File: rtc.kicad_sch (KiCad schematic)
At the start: 3 parts, among them U401 DS3231MZ

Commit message: SH-RPi v2 schematic design
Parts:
- removed BT401: CR1220/3V, SH-RPi:BatteryHolder_Myoung_MY-1220-03, symbol Connector_Generic:Conn_01x03
- removed U401: DS3231MZ, Package_SO:SOIC-8_3.9x4.9mm_P1.27mm, symbol Timer_RTC:DS3231MZ
- added BT801: Battery_Cell, symbol Device:Battery_Cell
- added C801: 1uF, symbol Device:C
- added C802: 22pF C0G, symbol Device:C_Small
- added D801, D802: 1N4148WS, Diode_SMD:D_SOD-323, symbol Device:D
- added JP801: SolderJumper_2_Bridged, symbol Jumper:SolderJumper_2_Bridged
- added U801: PCF8563T, Package_SO:SOIC-8_3.9x4.9mm_P1.27mm, symbol Timer_RTC:PCF8563T
- added Y801: X1A000061000200, Crystal:Crystal_SMD_2012-2Pin_2.0x1.2mm, symbol Device:Crystal
- renumbered C401 to C803
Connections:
- net GND: now also BT801.2 (-), C801.2, C802.1, U801.4 (VSS)
- net RTC_INT: now also U801.3 (~{INT})
- net SCL: now also U801.6 (SCL)
- net SDA: now also U801.5 (SDA)
- net VBAT: now also BT801.1 (+), C801.1, D802.2 (A)
- net ATT_Vcc: no longer names the net of C803.1
- net ATT_Vcc: now also D801.1 (K), D802.1 (K), U801.8 (VDD)
- new net: C802.2, U801.1 (OSCI), Y801.2
- new net: D801.2 (A), JP801.2 (B)
- new net: U801.2 (OSCO), Y801.1
- new net +3V3: JP801.1 (A)
- no-connect marks 3 -> 1

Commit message: WIP: Assign footprints and LCSC part numbers
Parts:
- C801: footprint (none) -> Capacitor_SMD:C_0402_1005Metric; LCSC (none) -> C52923
- C802: footprint (none) -> Capacitor_SMD:C_0402_1005Metric; LCSC (none) -> C1555
- JP801: footprint (none) -> Jumper:SolderJumper-2_P1.3mm_Bridged_Pad1.0x1.5mm
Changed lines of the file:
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@@
     (property "Reference" "C802" (id 0) (at 100.3363 85.09 90))
     (property "Value" "22pF C0G" (id 1) (at 100.3363 87.63 90))
-    (property "Footprint" "" (id 2) (at 100.33 91.44 0)
+    (property "Footprint" "Capacitor_SMD:C_0402_1005Metric" (id 2) (at 100.33 91.44 0)
       (effects (font (size 1.27 1.27)) hide)
     )
     (property "Datasheet" "~" (id 3) (at 100.33 91.44 0)
+      (effects (font (size 1.27 1.27)) hide)
+    )
+    (property "LCSC" "C1555" (id 4) (at 100.33 91.44 0)
       (effects (font (size 1.27 1.27)) hide)
     )
@@
       (effects (font (size 1.27 1.27)) (justify left))
     )
-    (property "Footprint" "" (id 2) (at 51.7652 100.33 0)
+    (property "Footprint" "Capacitor_SMD:C_0402_1005Metric" (id 2) (at 51.7652 100.33 0)
       (effects (font (size 1.27 1.27)) hide)
     )
     (property "Datasheet" "~" (id 3) (at 50.8 96.52 0)
+      (effects (font (size 1.27 1.27)) hide)
+    )
+    (property "LCSC" "C52923" (id 4) (at 50.8 96.52 0)
       (effects (font (size 1.27 1.27)) hide)
     )
@@
     (property "Reference" "JP801" (id 0) (at 92.71 69.85 0))
     (property "Value" "SolderJumper_2_Bridged" (id 1) (at 92.71 72.39 0))
-    (property "Footprint" "" (id 2) (at 92.71 76.2 0)
+    (property "Footprint" "Jumper:SolderJumper-2_P1.3mm_Bridged_Pad1.0x1.5mm" (id 2) (at 92.71 76.2 0)
       (effects (font (size 1.27 1.27)) hide)
     )

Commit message: Use a battery clip instead of a cell
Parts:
- removed BT801: Battery_Cell, symbol Device:Battery_Cell
- added J801: Conn_01x03, SH-RPi:BatteryHolder_Myoung_MY-1220-03, symbol Connector_Generic:Conn_01x03
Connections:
- net GND: now also J801.3 (Pin_3)
- net VBAT: now also J801.1 (Pin_1), J801.2 (Pin_2)
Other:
- note added: "CR1220 battery"
- note added: "Cut the solder jumper to disable RTC"
- moved on the sheet: C801
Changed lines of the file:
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@@
     (comment 3 "Sailor Hat for Raspberry Pi is licensed under CC BY 4.0.")
   )
+  (junction (at 60.96 91.44) (diameter 0) (color 0 0 0 0)
+  )
   (junction (at 74.93 83.82) (diameter 0) (color 0 0 0 0)
   )
@@
   (junction (at 106.68 91.44) (diameter 0) (color 0 0 0 0)
   )
-  (junction (at 60.96 91.44) (diameter 0) (color 0 0 0 0)
-  )
   (junction (at 127 80.01) (diameter 0) (color 0 0 0 0)
   )
+  (junction (at 73.66 91.44) (diameter 0) (color 0 0 0 0)
+  )
   (no_connect (at 137.16 99.06))
+  (wire (pts (xy 57.15 93.98) (xy 60.96 93.98))
+    (stroke (width 0) (type default) (color 0 0 0 0))
+  )
   (wire (pts (xy 110.49 80.01) (xy 74.93 80.01))
     (stroke (width 0) (type default) (color 0 0 0 0))
@@
     (stroke (width 0) (type default) (color 0 0 0 0))
   )
-  (wire (pts (xy 60.96 99.06) (xy 60.96 102.87))
+  (wire (pts (xy 60.96 96.52) (xy 60.96 102.87))
     (stroke (width 0) (type default) (color 0 0 0 0))
   )
@@
     (stroke (width 0) (type default) (color 0 0 0 0))
   )
-  (wire (pts (xy 50.8 91.44) (xy 60.96 91.44))
+  (wire (pts (xy 57.15 91.44) (xy 60.96 91.44))
     (stroke (width 0) (type default) (color 0 0 0 0))
   )
@@
     (stroke (width 0) (type default) (color 0 0 0 0))
   )
-  (wire (pts (xy 50.8 100.33) (xy 50.8 102.87))
+  (wire (pts (xy 73.66 100.33) (xy 73.66 102.87))
     (stroke (width 0) (type default) (color 0 0 0 0))
   )
@@
     (stroke (width 0) (type default) (color 0 0 0 0))
   )
-  (wire (pts (xy 60.96 91.44) (xy 74.93 91.44))
-    (stroke (width 0) (type default) (color 0 0 0 0))
-  )
   (wire (pts (xy 144.78 101.6) (xy 137.16 101.6))
     (stroke (width 0) (type default) (color 0 0 0 0))
@@
     (stroke (width 0) (type default) (color 0 0 0 0))
   )
+  (wire (pts (xy 73.66 91.44) (xy 74.93 91.44))
+    (stroke (width 0) (type default) (color 0 0 0 0))
+  )
   (wire (pts (xy 132.08 76.2) (xy 128.27 76.2))
     (stroke (width 0) (type default) (color 0 0 0 0))
@@
     (stroke (width 0) (type default) (color 0 0 0 0))
   )
+  (wire (pts (xy 60.96 91.44) (xy 73.66 91.44))
+    (stroke (width 0) (type default) (color 0 0 0 0))
+  )
+  (wire (pts (xy 60.96 93.98) (xy 60.96 91.44))
+    (stroke (width 0) (type default) (color 0 0 0 0))
+  )
   (wire (pts (xy 118.11 80.01) (xy 127 80.01))
     (stroke (width 0) (type default) (color 0 0 0 0))
@@
     (stroke (width 0) (type default) (color 0 0 0 0))
   )
-  (wire (pts (xy 50.8 92.71) (xy 50.8 91.44))
+  (wire (pts (xy 73.66 92.71) (xy 73.66 91.44))
     (stroke (width 0) (type default) (color 0 0 0 0))
   )
@@
   (wire (pts (xy 102.87 91.44) (xy 106.68 91.44))
     (stroke (width 0) (type default) (color 0 0 0 0))
+  )
+  (wire (pts (xy 57.15 96.52) (xy 60.96 96.52))
+    (stroke (width 0) (type default) (color 0 0 0 0))
+  )
+  (text "Cut the solder jumper\nto disable RTC" (at 85.09 64.77 0)
+    (effects (font (size 1.27 1.27)) (justify left bottom))
+  )
+  (text "CR1220 battery" (at 40.64 102.87 0)
+    (effects (font (size 1.27 1.27)) (justify left bottom))
   )
   (label "VBAT" (at 74.93 80.01 180)
@@
   (symbol (lib_id "power:GND") (at 60.96 102.87 0) (mirror y) (unit 1)
     (in_bom yes) (on_board yes)
-    (property "Reference" "#PWR0802" (id 0) (at 60.96 109.22 0)
+    (property "Reference" "#PWR0801" (id 0) (at 60.96 109.22 0)
       (effects (font (size 1.27 1.27)) hide)
     )
@@
     (pin "2")
   )
-  (symbol (lib_id "Device:C") (at 50.8 96.52 0) (unit 1)
-    (in_bom yes) (on_board yes) (fields_autoplaced)
-    (property "Reference" "C801" (id 0) (at 54.61 95.2499 0)
-      (effects (font (size 1.27 1.27)) (justify left))
-    )
-    (property "Value" "1uF" (id 1) (at 54.61 97.7899 0)
-      (effects (font (size 1.27 1.27)) (justify left))
-    )
-    (property "Footprint" "Capacitor_SMD:C_0402_1005Metric" (id 2) (at 51.7652 100.33 0)
-      (effects (font (size 1.27 1.27)) hide)
-    )
-    (property "Datasheet" "~" (id 3) (at 50.8 96.52 0)
-      (effects (font (size 1.27 1.27)) hide)
-    )
-    (property "LCSC" "C52923" (id 4) (at 50.8 96.52 0)
+  (symbol (lib_id "Device:C") (at 73.66 96.52 0) (unit 1)
+    (in_bom yes) (on_board yes) (fields_autoplaced)
+    (property "Reference" "C801" (id 0) (at 77.47 95.2499 0)
+      (effects (font (size 1.27 1.27)) (justify left))
+    )
+    (property "Value" "1uF" (id 1) (at 77.47 97.7899 0)
+      (effects (font (size 1.27 1.27)) (justify left))
+    )
+    (property "Footprint" "Capacitor_SMD:C_0402_1005Metric" (id 2) (at 74.6252 100.33 0)
+      (effects (font (size 1.27 1.27)) hide)
+    )
+    (property "Datasheet" "~" (id 3) (at 73.66 96.52 0)
+      (effects (font (size 1.27 1.27)) hide)
+    )
+    (property "LCSC" "C52923" (id 4) (at 73.66 96.52 0)
       (effects (font (size 1.27 1.27)) hide)
     )
@@
     (pin "8")
   )
-  (symbol (lib_id "power:GND") (at 50.8 102.87 0) (mirror y) (unit 1)
-    (in_bom yes) (on_board yes)
-    (property "Reference" "#PWR0801" (id 0) (at 50.8 109.22 0)
-      (effects (font (size 1.27 1.27)) hide)
-    )
-    (property "Value" "GND" (id 1) (at 50.673 107.2642 0))
-    (property "Footprint" "" (id 2) (at 50.8 102.87 0)
-      (effects (font (size 1.27 1.27)) hide)
-    )
-    (property "Datasheet" "" (id 3) (at 50.8 102.87 0)
+  (symbol (lib_id "power:GND") (at 73.66 102.87 0) (mirror y) (unit 1)
+    (in_bom yes) (on_board yes)
+    (property "Reference" "#PWR0802" (id 0) (at 73.66 109.22 0)
+      (effects (font (size 1.27 1.27)) hide)
+    )
+    (property "Value" "GND" (id 1) (at 73.533 107.2642 0))
+    (property "Footprint" "" (id 2) (at 73.66 102.87 0)
+      (effects (font (size 1.27 1.27)) hide)
+    )
+    (property "Datasheet" "" (id 3) (at 73.66 102.87 0)
       (effects (font (size 1.27 1.27)) hide)
     )
@@
     )
     (pin "1")
+  )
+  (symbol (lib_id "Connector_Generic:Conn_01x03") (at 52.07 93.98 0) (mirror y) (unit 1)
+    (in_bom yes) (on_board yes) (fields_autoplaced)
+    (property "Reference" "J801" (id 0) (at 52.07 85.09 0))
+    (property "Value" "Conn_01x03" (id 1) (at 52.07 87.63 0))
+    (property "Footprint" "SH-RPi:BatteryHolder_Myoung_MY-1220-03" (id 2) (at 52.07 93.98 0)
+      (effects (font (size 1.27 1.27)) hide)
+    )
+    (property "Datasheet" "~" (id 3) (at 52.07 93.98 0)
+      (effects (font (size 1.27 1.27)) hide)
+    )
+    (property "LCSC" "C964818" (id 4) (at 52.07 93.98 0)
+      (effects (font (size 1.27 1.27)) hide)
+    )
+    (pin "1")
+    (pin "2")
+    (pin "3")
   )
   (symbol (lib_id "power:PWR_FLAG") (at 128.27 76.2 0) (unit 1)
@@
     (pin "1")
   )
-  (symbol (lib_id "Device:Battery_Cell") (at 60.96 96.52 0) (unit 1)
-    (in_bom yes) (on_board yes) (fields_autoplaced)
-    (property "Reference" "BT801" (id 0) (at 64.77 93.2179 0)
-      (effects (font (size 1.27 1.27)) (justify left))
-    )
-    (property "Value" "Battery_Cell" (id 1) (at 64.77 95.7579 0)
-      (effects (font (size 1.27 1.27)) (justify left))
-    )
-    (property "Footprint" "" (id 2) (at 60.96 94.996 90)
-      (effects (font (size 1.27 1.27)) hide)
-    )
-    (property "Datasheet" "~" (id 3) (at 60.96 94.996 90)
-      (effects (font (size 1.27 1.27)) hide)
-    )
-    (pin "1")
-    (pin "2")
-  )
 )

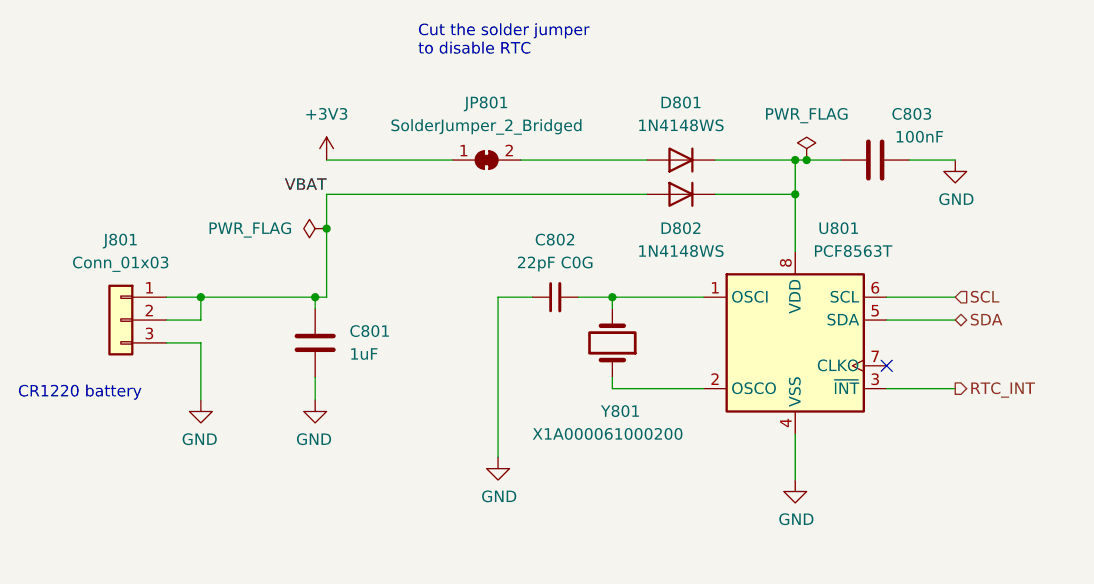
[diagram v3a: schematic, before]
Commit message: Assign footprints and part numbers to components
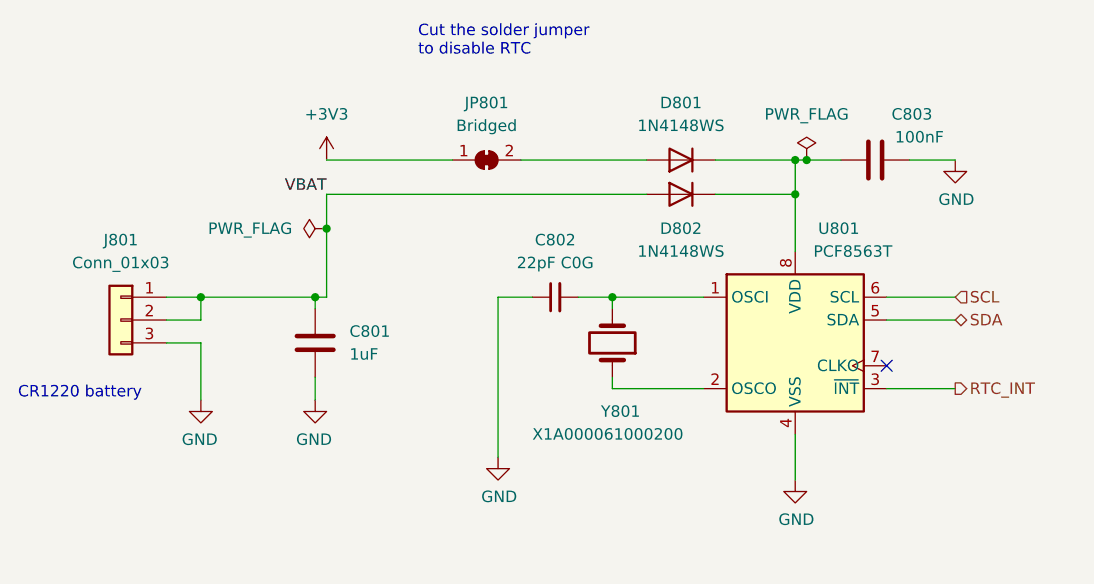
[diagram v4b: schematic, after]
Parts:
- JP801: value SolderJumper_2_Bridged -> Bridged
- U801: LCSC (none) -> C7440
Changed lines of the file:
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@@
     (in_bom yes) (on_board yes) (fields_autoplaced)
     (property "Reference" "JP801" (id 0) (at 92.71 69.85 0))
-    (property "Value" "SolderJumper_2_Bridged" (id 1) (at 92.71 72.39 0))
+    (property "Value" "Bridged" (id 1) (at 92.71 72.39 0))
     (property "Footprint" "Jumper:SolderJumper-2_P1.3mm_Bridged_Pad1.0x1.5mm" (id 2) (at 92.71 76.2 0)
       (effects (font (size 1.27 1.27)) hide)
@@
       (effects (font (size 1.27 1.27)) hide)
     )
+    (property "LCSC" "C7440" (id 4) (at 127 96.52 0)
+      (effects (font (size 1.27 1.27)) hide)
+    )

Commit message: WIP: PCB layout
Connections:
- net RTCVDD: now reaches C803.1, D801.1 (K), D802.1 (K), U801.8 (VDD)
- net OSCI: now reaches C802.2, U801.1 (OSCI), Y801.2
- net OSCO: now reaches U801.2 (OSCO), Y801.1
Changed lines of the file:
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@@
     (effects (font (size 1.27 1.27)) (justify left bottom))
+  )
+  (label "OSCO" (at 114.3 101.6 180)
+    (effects (font (size 1.27 1.27)) (justify right bottom))
   )
   (label "VBAT" (at 74.93 80.01 180)
     (effects (font (size 1.27 1.27)) (justify right bottom))
   )
+  (label "OSCI" (at 114.3 91.44 180)
+    (effects (font (size 1.27 1.27)) (justify right bottom))
+  )
+  (label "RTCVDD" (at 127 83.82 180)
+    (effects (font (size 1.27 1.27)) (justify right bottom))
+  )

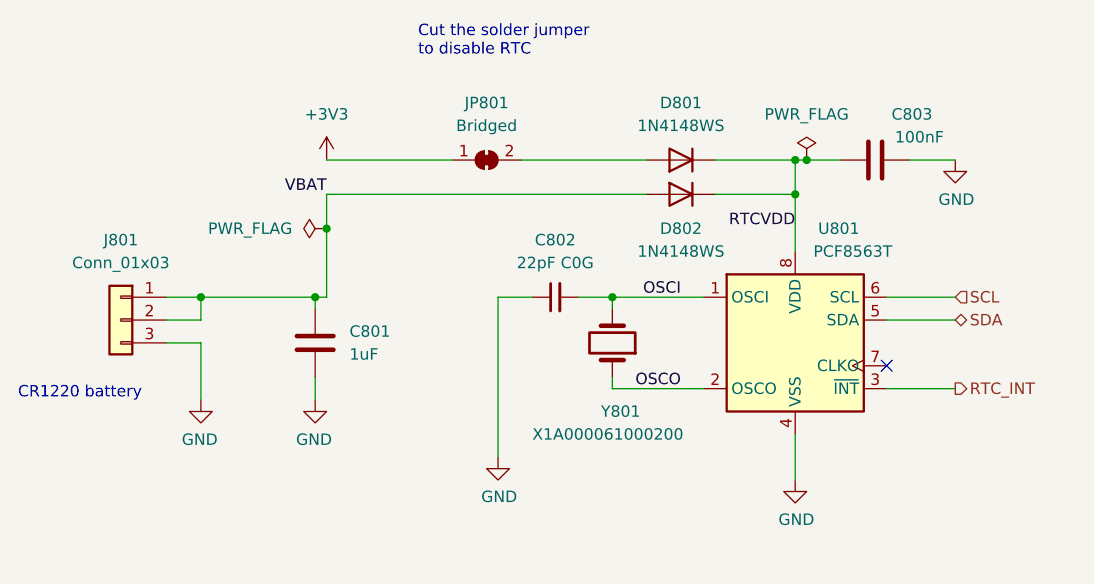
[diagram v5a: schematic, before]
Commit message: Initial PCB component layout done
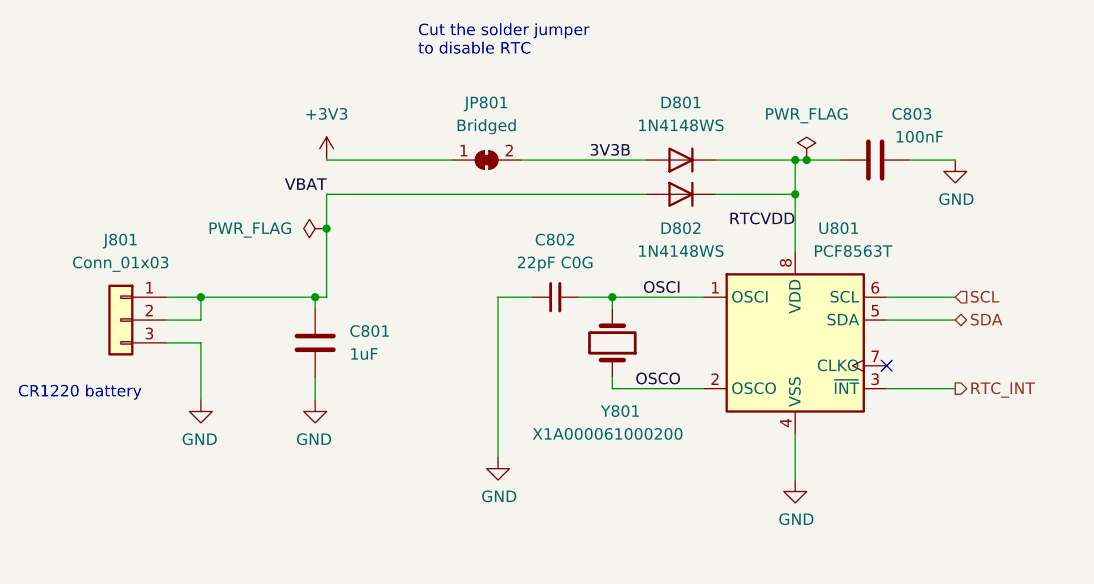
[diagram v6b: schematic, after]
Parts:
- U801: symbol Timer_RTC:PCF8563T -> SH-RPi:PCF8563T
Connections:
- net 3V3B: now reaches D801.2 (A), JP801.2 (B)
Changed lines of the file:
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@@
+    (effects (font (size 1.27 1.27)) (justify left bottom))
+  )
+  (label "3V3B" (at 104.14 76.2 0)
     (effects (font (size 1.27 1.27)) (justify left bottom))
   )
@@
     (pin "2")
   )
-  (symbol (lib_id "Timer_RTC:PCF8563T") (at 127 96.52 0) (unit 1)
+  (symbol (lib_id "SH-RPi:PCF8563T") (at 127 96.52 0) (unit 1)
     (in_bom yes) (on_board yes)
     (property "Reference" "U801" (id 0) (at 129.54 83.82 0)

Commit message: Finish PCB routing
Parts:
- C802: footprint Capacitor_SMD:C_0402_1005Metric -> Capacitor_SMD:C_0603_1608Metric; LCSC C1555 -> C1653
- JP801: footprint Jumper:SolderJumper-2_P1.3mm_Bridged_Pad1.0x1.5mm -> Jumper:SolderJumper-2_P1.3mm_Bridged2Bar_RoundedPad1.0x1.5mm
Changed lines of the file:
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@@
     (property "Reference" "C802" (id 0) (at 100.3363 85.09 90))
     (property "Value" "22pF C0G" (id 1) (at 100.3363 87.63 90))
-    (property "Footprint" "Capacitor_SMD:C_0402_1005Metric" (id 2) (at 100.33 91.44 0)
+    (property "Footprint" "Capacitor_SMD:C_0603_1608Metric" (id 2) (at 100.33 91.44 0)
       (effects (font (size 1.27 1.27)) hide)
     )
@@
       (effects (font (size 1.27 1.27)) hide)
     )
-    (property "LCSC" "C1555" (id 4) (at 100.33 91.44 0)
+    (property "LCSC" "C1653" (id 4) (at 100.33 91.44 0)
       (effects (font (size 1.27 1.27)) hide)
     )
@@
     (property "Reference" "JP801" (id 0) (at 92.71 69.85 0))
     (property "Value" "Bridged" (id 1) (at 92.71 72.39 0))
-    (property "Footprint" "Jumper:SolderJumper-2_P1.3mm_Bridged_Pad1.0x1.5mm" (id 2) (at 92.71 76.2 0)
+    (property "Footprint" "Jumper:SolderJumper-2_P1.3mm_Bridged2Bar_RoundedPad1.0x1.5mm" (id 2) (at 92.71 76.2 0)
       (effects (font (size 1.27 1.27)) hide)
     )

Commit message: Replace "ideal diode" with Schottky & other changes
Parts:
- JP801: footprint Jumper:SolderJumper-2_P1.3mm_Bridged2Bar_RoundedPad1.0x1.5mm -> Jumper:SolderJumper-2_P1.3mm_Bridged2Bar_Pad1.0x1.5mm
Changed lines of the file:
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@@
   (title_block
     (title "Sailor Hat for Raspberry Pi")
-    (date "2022-10-14")
-    (rev "v2.0.0-alpha")
+    (date "2022-10-21")
+    (rev "v2.0.0-a1")
     (company "Hat Labs Ltd")
     (comment 1 "https://creativecommons.org/licenses/by/4.0")
@@
     (property "Reference" "JP801" (id 0) (at 92.71 69.85 0))
     (property "Value" "Bridged" (id 1) (at 92.71 72.39 0))
-    (property "Footprint" "Jumper:SolderJumper-2_P1.3mm_Bridged2Bar_RoundedPad1.0x1.5mm" (id 2) (at 92.71 76.2 0)
-      (effects (font (size 1.27 1.27)) hide)
-    )
+    (property "Footprint" "Jumper:SolderJumper-2_P1.3mm_Bridged2Bar_Pad1.0x1.5mm" (id 2) (at 92.71 76.2 0)
+      (effects (font (size 1.27 1.27)) hide)
+    )
